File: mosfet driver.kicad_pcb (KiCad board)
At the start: 2 copper layers, 47 x 74.9 mm, 23 parts, among them J1 Screw_Terminal_01x03, J2 Screw_Terminal_01x02, J3 Conn_01x03_Male, Q1 IRF3205, Q2 IRF3205, Q3 IRF3205, Q4 IRF3205, U1 IR2104, U2 IR2104

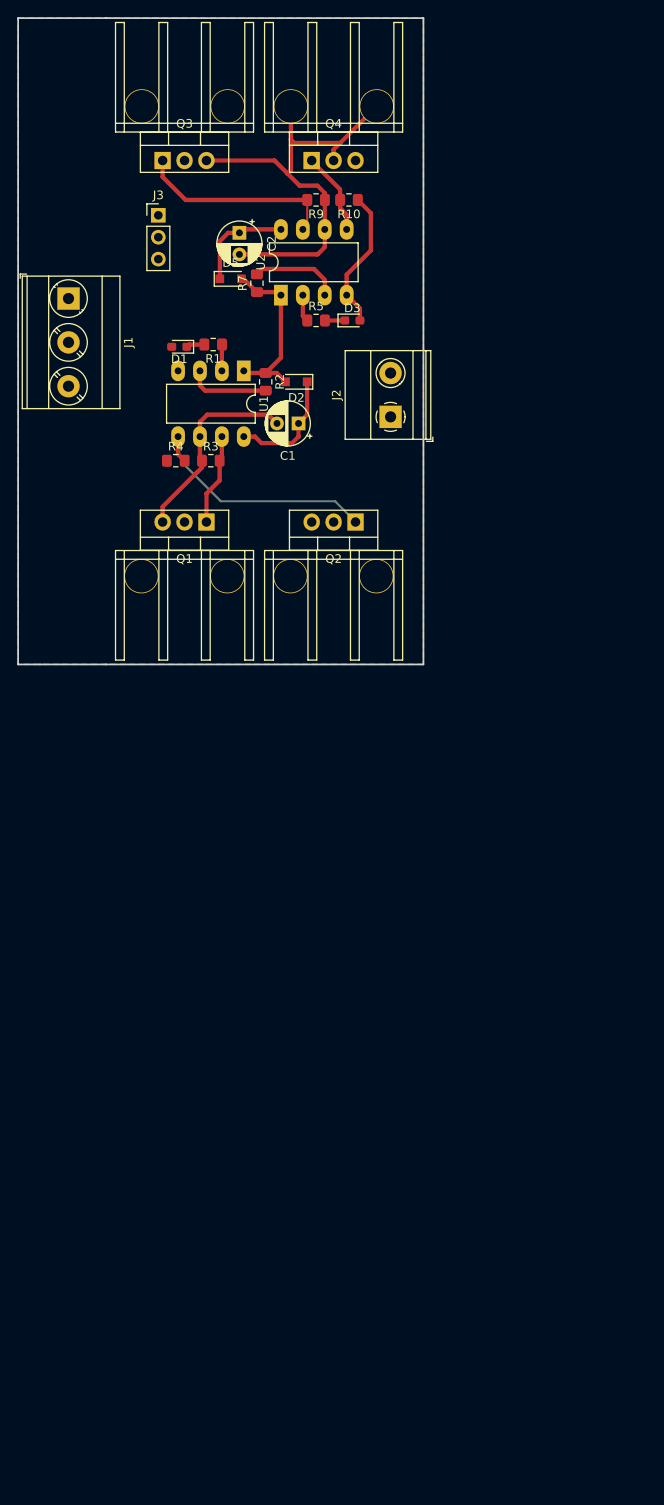
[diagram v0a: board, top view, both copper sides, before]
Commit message: Current Sensor placement solved
Switch for current sensor added for bypassing it whenever unnecessary. This board is also tailored for manufacturing in-house.
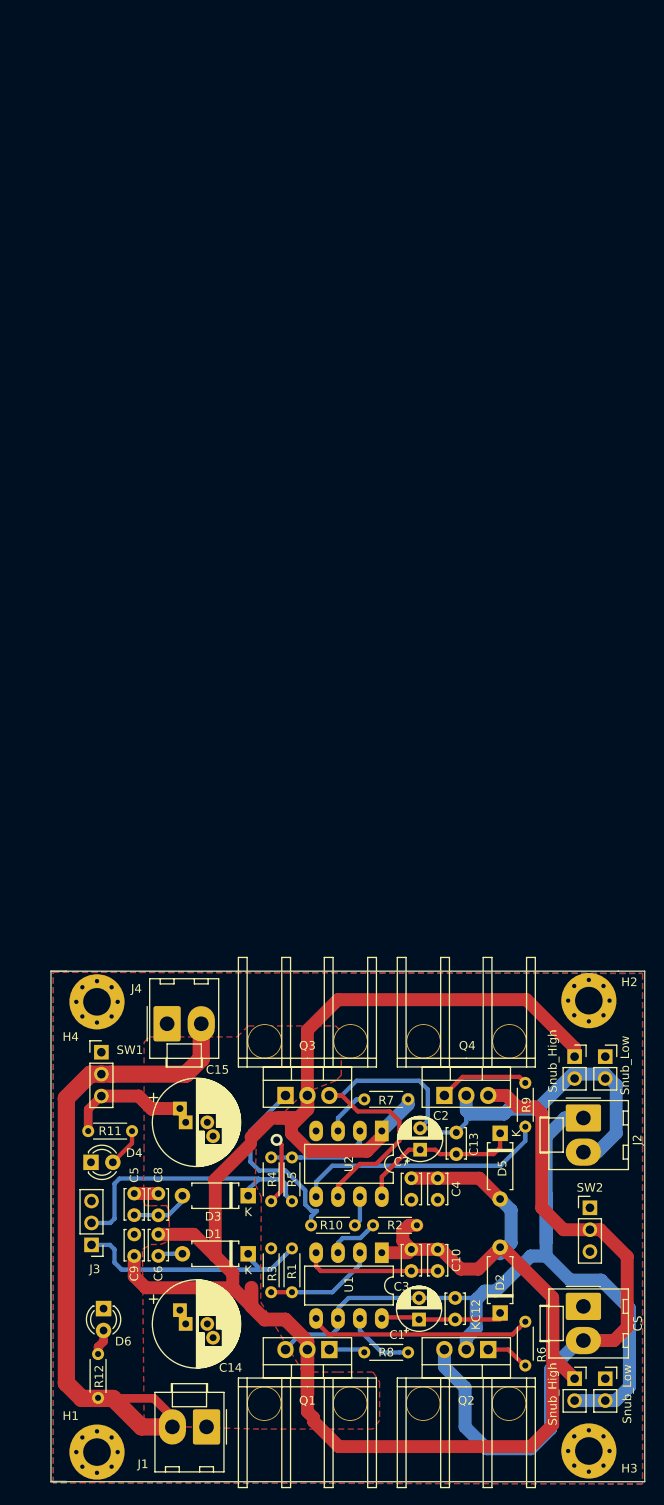
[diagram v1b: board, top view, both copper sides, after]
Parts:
- added C10: 1uF, Capacitor_THT:C_Disc_D3.4mm_W2.1mm_P2.50mm, F.Cu at (86.7, 155.4)
- added C12: 0.1uF, Capacitor_THT:C_Disc_D3.4mm_W2.1mm_P2.50mm, F.Cu at (88.8, 163.6)
- added C13: 0.1uF, Capacitor_THT:C_Disc_D3.4mm_W2.1mm_P2.50mm, F.Cu at (88.9, 144.4)
- added C14: 270uF/35V, Capacitor_THT:CP_Radial_D10.0mm_P2.50mm_P5.00mm, F.Cu at (57.5, 164.1)
- added C15: 270uF/35V, Capacitor_THT:CP_Radial_D10.0mm_P2.50mm_P5.00mm, F.Cu at (57.5, 140.7)
- added C3: 0.1uF, Capacitor_THT:C_Disc_D3.4mm_W2.1mm_P2.50mm, F.Cu at (83.7, 155.4)
- added C4: 0.1uF, Capacitor_THT:C_Disc_D3.4mm_W2.1mm_P2.50mm, F.Cu at (86.7, 147.2)
- added C5: 0.1uF, Capacitor_THT:C_Disc_D3.4mm_W2.1mm_P2.50mm, F.Cu at (51.6, 149.0)
- added C6: 0.1uF, Capacitor_THT:C_Disc_D3.4mm_W2.1mm_P2.50mm, F.Cu at (54.4, 153.7)
- added C7: 1uF, Capacitor_THT:C_Disc_D3.4mm_W2.1mm_P2.50mm, F.Cu at (83.7, 147.2)
- added C8: 1uF, Capacitor_THT:C_Disc_D3.4mm_W2.1mm_P2.50mm, F.Cu at (54.4, 149.0)
- added C9: 1uF, Capacitor_THT:C_Disc_D3.4mm_W2.1mm_P2.50mm, F.Cu at (51.6, 156.2)
- added CS: Molex_KK-396_A-41791-0002_1x02_P3.96mm_Vertical, MOLEX Footprints:Molex_KK-396_A-41791-0002_1x02_P3.96mm_Vertical, F.Cu at (103.6, 162.1)
- added D4: LED, LED_THT:LED_D3.0mm, F.Cu at (46.5, 145.4)
- added D6: LED, LED_THT:LED_D3.0mm, F.Cu at (48.0, 162.3)
- added H1: MountingHole, MountingHole:MountingHole_3.2mm_M3_Pad_Via, F.Cu at (47.2, 178.9)
- added H2: MountingHole, MountingHole:MountingHole_3.2mm_M3_Pad_Via, F.Cu at (104.3, 126.6)
- added H3: MountingHole, MountingHole:MountingHole_3.2mm_M3_Pad_Via, F.Cu at (104.3, 178.8)
- added H4: MountingHole, MountingHole:MountingHole_3.2mm_M3_Pad_Via, F.Cu at (47.2, 126.7)
- added J4: PWR_IN, Connector_Molex:Molex_KK-396_A-41791-0002_1x02_P3.96mm_Vertical, F.Cu at (55.4, 129.3)
- added R11: 1k, Resistor_THT:R_Axial_DIN0204_L3.6mm_D1.6mm_P5.08mm_Horizontal, F.Cu at (46.2, 141.7)
- added R12: 1k, Resistor_THT:R_Axial_DIN0204_L3.6mm_D1.6mm_P5.08mm_Horizontal, F.Cu at (47.4, 172.7)
- added R6: 10, Resistor_THT:R_Axial_DIN0204_L3.6mm_D1.6mm_P5.08mm_Horizontal, F.Cu at (96.9, 163.8)
- added R8: 10, Resistor_THT:R_Axial_DIN0204_L3.6mm_D1.6mm_P5.08mm_Horizontal, F.Cu at (78.2, 167.4)
- added SW1: SW_DIP_x01, Connector_PinHeader_2.54mm:PinHeader_1x03_P2.54mm_Vertical, F.Cu at (47.8, 132.6)
- added SW2: PinHeader_1x03_P2.54mm_Vertical, Connector_PinHeader_2.54mm:PinHeader_1x03_P2.54mm_Vertical, F.Cu at (104.4, 150.6)
- added Snub_High: PinSocket_1x02_P2.54mm_Vertical, Connector_PinSocket_2.54mm:PinSocket_1x02_P2.54mm_Vertical, F.Cu at (102.6, 170.4)
- added Snub_High: PinSocket_1x02_P2.54mm_Vertical, Connector_PinSocket_2.54mm:PinSocket_1x02_P2.54mm_Vertical, F.Cu at (102.6, 133.1)
- added Snub_Low: PinSocket_1x02_P2.54mm_Vertical, Connector_PinSocket_2.54mm:PinSocket_1x02_P2.54mm_Vertical, F.Cu at (106.2, 170.4)
- added Snub_Low: PinSocket_1x02_P2.54mm_Vertical, Connector_PinSocket_2.54mm:PinSocket_1x02_P2.54mm_Vertical, F.Cu at (106.2, 133.1)
- D1, D3: footprint Diode_SMD:D_0603_1608Metric_Pad1.05x0.95mm_HandSolder -> Diode_THT:D_A-405_P7.62mm_Horizontal
- D2, D5: footprint Diode_SMD:D_SOD-323_HandSoldering -> Diode_THT:D_A-405_P7.62mm_Horizontal
- J1: value Screw_Terminal_01x03 -> PWR_IN; footprint TerminalBlock_Phoenix:TerminalBlock_Phoenix_MKDS-3-3-5.08_1x03_P5.08mm_Horizontal -> Connector_Molex:Molex_KK-396_A-41791-0002_1x02_P3.96mm_Vertical
- J2: footprint TerminalBlock_Phoenix:TerminalBlock_Phoenix_MKDS-1,5-2-5.08_1x02_P5.08mm_Horizontal -> Connector_Molex:Molex_KK-396_A-41791-0002_1x02_P3.96mm_Vertical
- Q1, Q2, Q3, Q4: footprint mosfet_with_hest_sink:heatsink2 -> Heatsink:heatsinknew
- R1, R2, R5, R7: footprint Resistor_SMD:R_0805_2012Metric_Pad1.15x1.40mm_HandSolder -> Resistor_THT:R_Axial_DIN0204_L3.6mm_D1.6mm_P5.08mm_Horizontal
- R10, R3, R4, R9: value 1K -> 10; footprint Resistor_SMD:R_0805_2012Metric_Pad1.15x1.40mm_HandSolder -> Resistor_THT:R_Axial_DIN0204_L3.6mm_D1.6mm_P5.08mm_Horizontal
- moved J1 131.8 mm to (59.9, 176.0), turned to 180 degrees
- moved J3 119.6 mm to (46.6, 154.9), turned to 180 degrees
- moved R10 119.0 mm to (72.1, 152.7), turned to 0 degrees
- moved D2 110.5 mm to (94.0, 162.8), turned to 90 degrees
- moved R1 110.2 mm to (69.8, 160.4), turned to 90 degrees
- moved R9 110.1 mm to (96.9, 141.2), turned to 90 degrees
- moved Q4 109.5 mm to (87.5, 137.6)
- moved Q3 109.3 mm to (69.1, 137.6)
- moved C2 108.3 mm to (84.7, 143.9), turned to 90 degrees
- moved D1 105.5 mm to (64.8, 156.0)
- moved C1 104.8 mm to (84.6, 163.6), turned to 90 degrees
- moved D5 103.9 mm to (94.0, 142.0), turned to 270 degrees
- moved U1 103.5 mm to (80.3, 155.8)
- moved D3 102.2 mm to (64.8, 149.2), turned to 180 degrees
- moved R2 99.3 mm to (84.3, 152.7), turned to 180 degrees
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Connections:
- J1 pad 1: VCC -> GND
- J1 pad 2: GND -> Net-(J4-Pad2)
- Q2 pad 3: GND -> (no net)
- Q4 pad 3: GND -> (no net)
- R10 pad 1: GND -> Net-(Q3-Pad1)
- R10 pad 2: Net-(Q4-Pad1) -> Net-(R10-Pad2)
- R3 pad 1: /Power3 -> Net-(R1-Pad1)
- R3 pad 2: Net-(Q1-Pad1) -> GND
- R4 pad 1: GND -> Net-(R4-Pad1)
- R4 pad 2: Net-(Q2-Pad1) -> GND
- R5 pad 1: Net-(R5-Pad1) -> Net-(R4-Pad1)
- R9 pad 1: /Power4 -> Net-(R9-Pad1)
- R9 pad 2: Net-(Q3-Pad1) -> Net-(Q4-Pad1)
- U1 pad 5: Net-(Q2-Pad1) -> Net-(R6-Pad1)
- U1 pad 7: Net-(Q1-Pad1) -> Net-(R8-Pad2)
- U2 pad 2: Net-(R5-Pad1) -> Net-(R4-Pad1)
- U2 pad 5: Net-(Q4-Pad1) -> Net-(R9-Pad1)
- U2 pad 7: Net-(Q3-Pad1) -> Net-(R10-Pad2)
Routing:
- net VCC: track 20.5 -> 254.9 mm
- net Net-(J4-Pad2): track 0.00 -> 79.7 mm
- net (no net): track 0.00 -> 78.1 mm
- net /Power3: track 23.3 -> 95.3 mm
- net /Signal2: track 2.31 -> 32.7 mm
- net Net-(R9-Pad1): track 0.00 -> 29.8 mm
- net /Signal: track 2.14 -> 29.9 mm
- net /Power4: track 54.0 -> 80.0 mm
- net Net-(R6-Pad1): track 0.00 -> 25.9 mm
- net Net-(Q2-Pad1): track 25.9 -> 5.07 mm
- net GND: track 16.4 -> 32.7 mm, vias 0 -> 1
- net Net-(R4-Pad1): track 0.00 -> 12.3 mm
- net Net-(R1-Pad1): track 3.06 -> 13.0 mm
- net Net-(C13-Pad1): track 12.0 -> 20.6 mm
- net Net-(R8-Pad2): track 0.00 -> 8.04 mm
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- added copper zone on F.Cu, net VCC
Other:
- board size 47 x 74.9 mm -> 68.8 x 59.2 mm
- net class Default: trace_width 0.25 -> 0.5; via_dia 0.8 -> 1.2; via_drill 0.4 -> 0.8
- net class Ground added: clearance 0.2, trace_width 3.5, via_dia 3.5, via_drill 3.1
- net class Power added: clearance 0.4, trace_width 3.3, via_dia 3.5, via_drill 3.1
- rule trace_min: 0.2 -> 0.5
- rule via_min_size: 0.4 -> 1
- board text added: "H-Bridge MOSFET Driver (Using IR2104)"
- board text added: "VIIT Robotics (2020)"
